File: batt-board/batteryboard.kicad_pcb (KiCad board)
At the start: 2 copper layers, 95.9 x 90.2 mm, 30 parts, among them J1 KEYSTONE-1042, J10 Screw_Terminal_01x02, J11 Screw_Terminal_01x02, J12 Screw_Terminal_01x01, J2 KEYSTONE-1042, J3 KEYSTONE-1042, J4 KEYSTONE-1042, J7 JST_PH_S2B-PH-SM4, J8 Screw_Terminal_01x02, J9 Screw_Terminal_01x02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

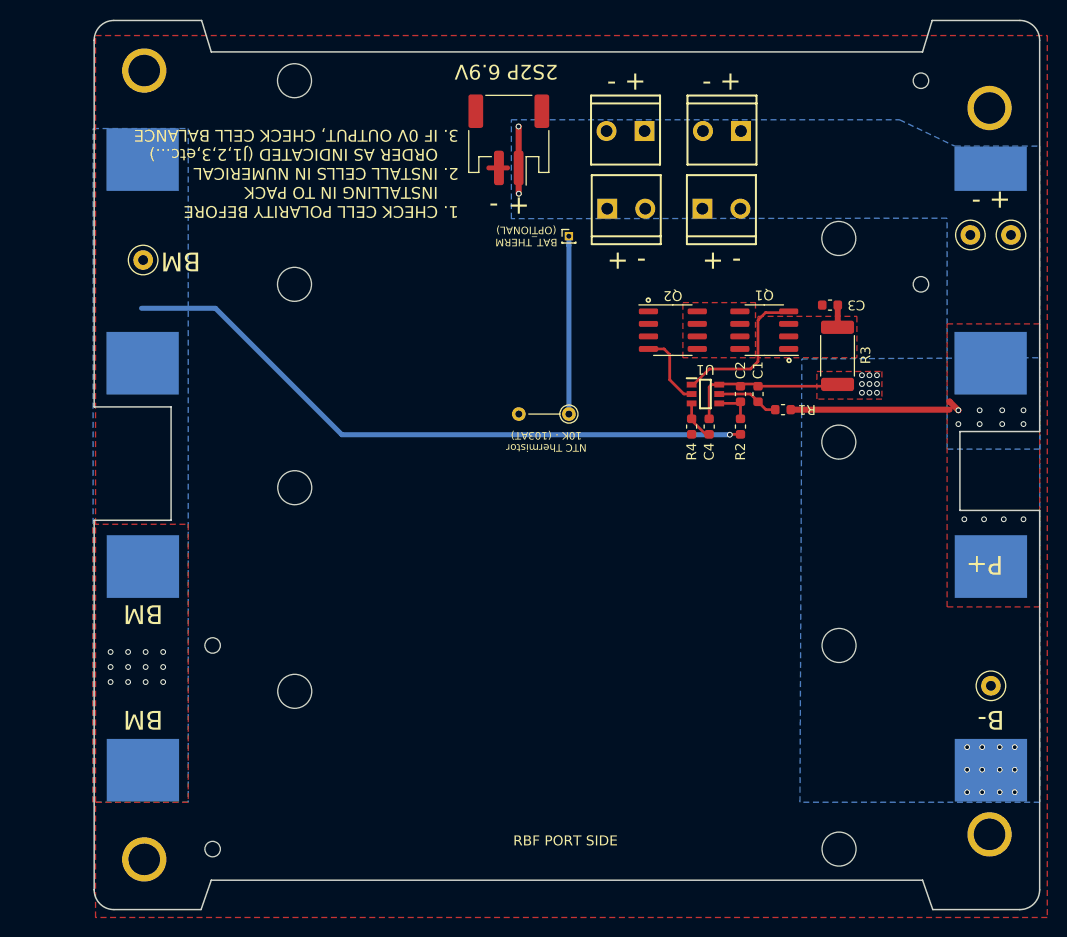
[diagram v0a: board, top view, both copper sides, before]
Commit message: rotated JST, fixed batt holder holes
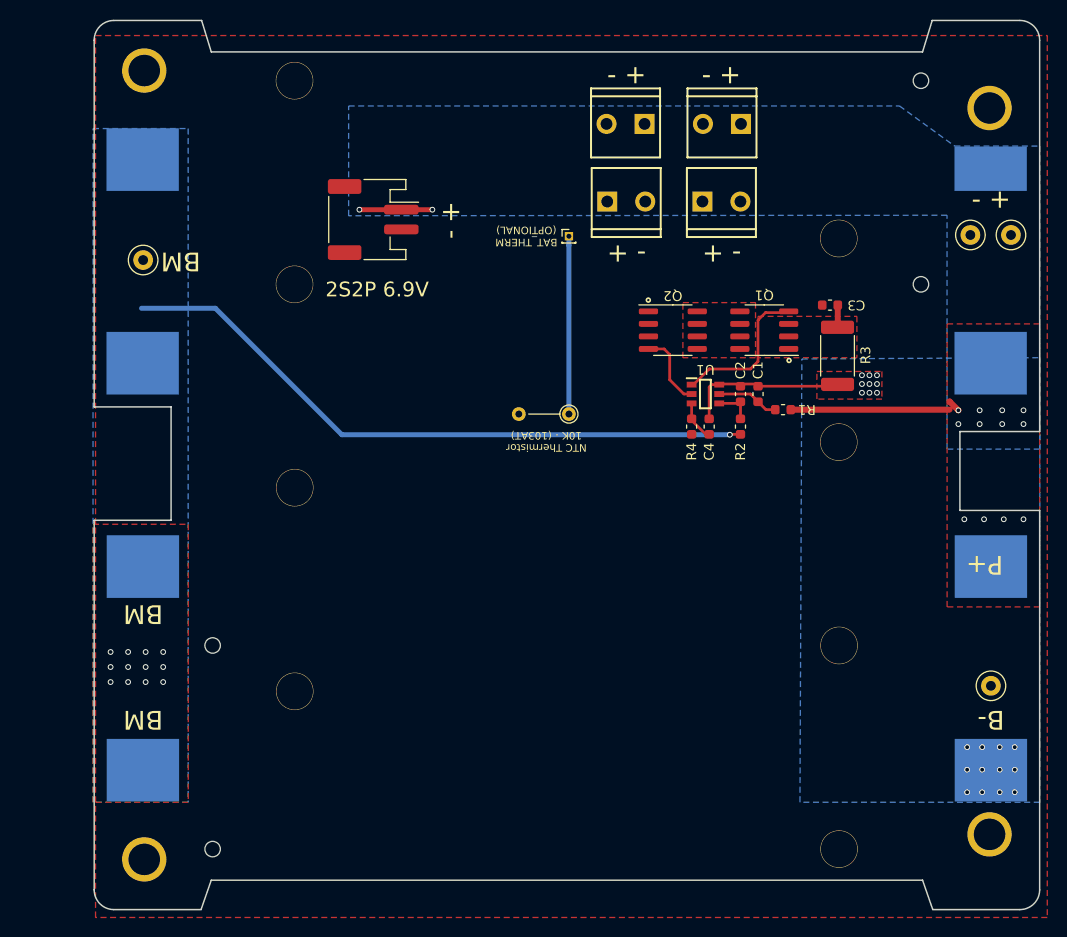
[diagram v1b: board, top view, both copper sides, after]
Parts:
- moved J7 16.0 mm to (81.5, 74.0), turned to -90 degrees
- moved J10 0.72 mm to (118.6, 64.3)
- moved J8 0.72 mm to (108.8, 64.3)
- moved J11 0.72 mm to (115.1, 72.2)
- moved J9 0.72 mm to (105.4, 72.2)
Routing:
- net PACK-: track 1.91 -> 0.00 mm
- net PACK+: track 24.2 -> 24.8 mm
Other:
- board text removed: "1. CHECK CELL POLARITY BEFORE INSTALLING IN TO PACK 2. INSTALL CELLS IN NUMERICAL ORDER AS INDICATED (J1,2,3,etc...) 3. IF 0V OUTPUT, CHECK CELL BALANCE"
- board text removed: "RBF PORT SIDE"

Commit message: new batt board and bottom adapter w/ fixed silkscreen
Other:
- board text added: "2S2P"
- board text added: "THE TEAM Alex Kelso|Kavitha Rau|Emily Hsieh Alex Xu|Ethan Philpott|Dara Wang Alan Hentrich|Mateo Graziosi Sebastian Abreu|N'kira Brooks Thomas Cuvillier|Eva Ahmetaj Hanif Bhatti|Chris Tian Chris Glenn|Melissa Garcia Ospina Ethan Taub|Aiden Guo|JC Guerrero Sheffield Wang|Jihan Shende Neil Kumar|Momoe Nomoto Sean Mo|Zijie Wu|Luke Adrianzen Kevin Park|Irvin Chadraa Gabrielle Phillips|Shuhe Ma Victor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"
- board text removed: "2S2P 6.9V"
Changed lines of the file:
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@@
   (gr_circle (center 123.6726 88.2904) (end 123.7488 88.3158) (layer "F.SilkS") (width 0.4) (fill none))
   (gr_circle (center 109.3978 82.169) (end 109.474 82.1944) (layer "F.SilkS") (width 0.4) (fill none))
+  (gr_rect (start 83.82 99.06) (end 119.38 137.16) (layer "F.SilkS") (width 0.127) (fill none))
   (gr_arc (start 55.2003 143.9799) (mid 53.786086 143.394114) (end 53.2003 141.9799) (layer "Edge.Cuts") (width 0.15))
   (gr_arc (start 149.0853 141.9799) (mid 148.499514 143.394114) (end 147.0853 143.9799) (layer "Edge.Cuts") (width 0.15))
@@
     (effects (font (size 0.762 0.762) (thickness 0.127)))
   )
-  (gr_text "2S2P 6.9V" (at 81.9 81.1) (layer "F.SilkS")
+  (gr_text "2S2P" (at 81.9 81.1) (layer "F.SilkS")
     (effects (font (size 1.5 1.5) (thickness 0.355)))
   )
@@
     (effects (font (size 1.905 1.905) (thickness 0.381)))
   )
+  (gr_text "THE TEAM\n\nAlex Kelso|Kavitha Rau|Emily Hsieh\nAlex Xu|Ethan Philpott|Dara Wang\nAlan Hentrich|Mateo Graziosi\nSebastian Abreu|N'kira Brooks\nThomas Cuvillier|Eva Ahmetaj\nHanif Bhatti|Chris Tian\nChris Glenn|Melissa Garcia Ospina\nEthan Taub|Aiden Guo|JC Guerrero\nSheffield Wang|Jihan Shende\nNeil Kumar|Momoe Nomoto\nSean Mo|Zijie Wu|Luke Adrianzen\nKevin Park|Irvin Chadraa\nGabrielle Phillips|Shuhe Ma\nVictor Rego|Jiayu Chen\nEhtisham Chaudhary|Rashik Ahmed\nMichael Xu|Tina Chibane\n\n" (at 101.6 119.38) (layer "F.SilkS")
+    (effects (font (size 1.2 1.2) (thickness 0.15)))
+  )
   (gr_text "BM" (at 58.166 114 180) (layer "F.SilkS")
